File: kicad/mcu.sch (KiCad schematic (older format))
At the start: 35 parts, among them J4 UEXT, J7 6P6C, J8 ST_Nucleo_SWD_5p, U1 STM32L072CZTx, U4 D1213A-04SO

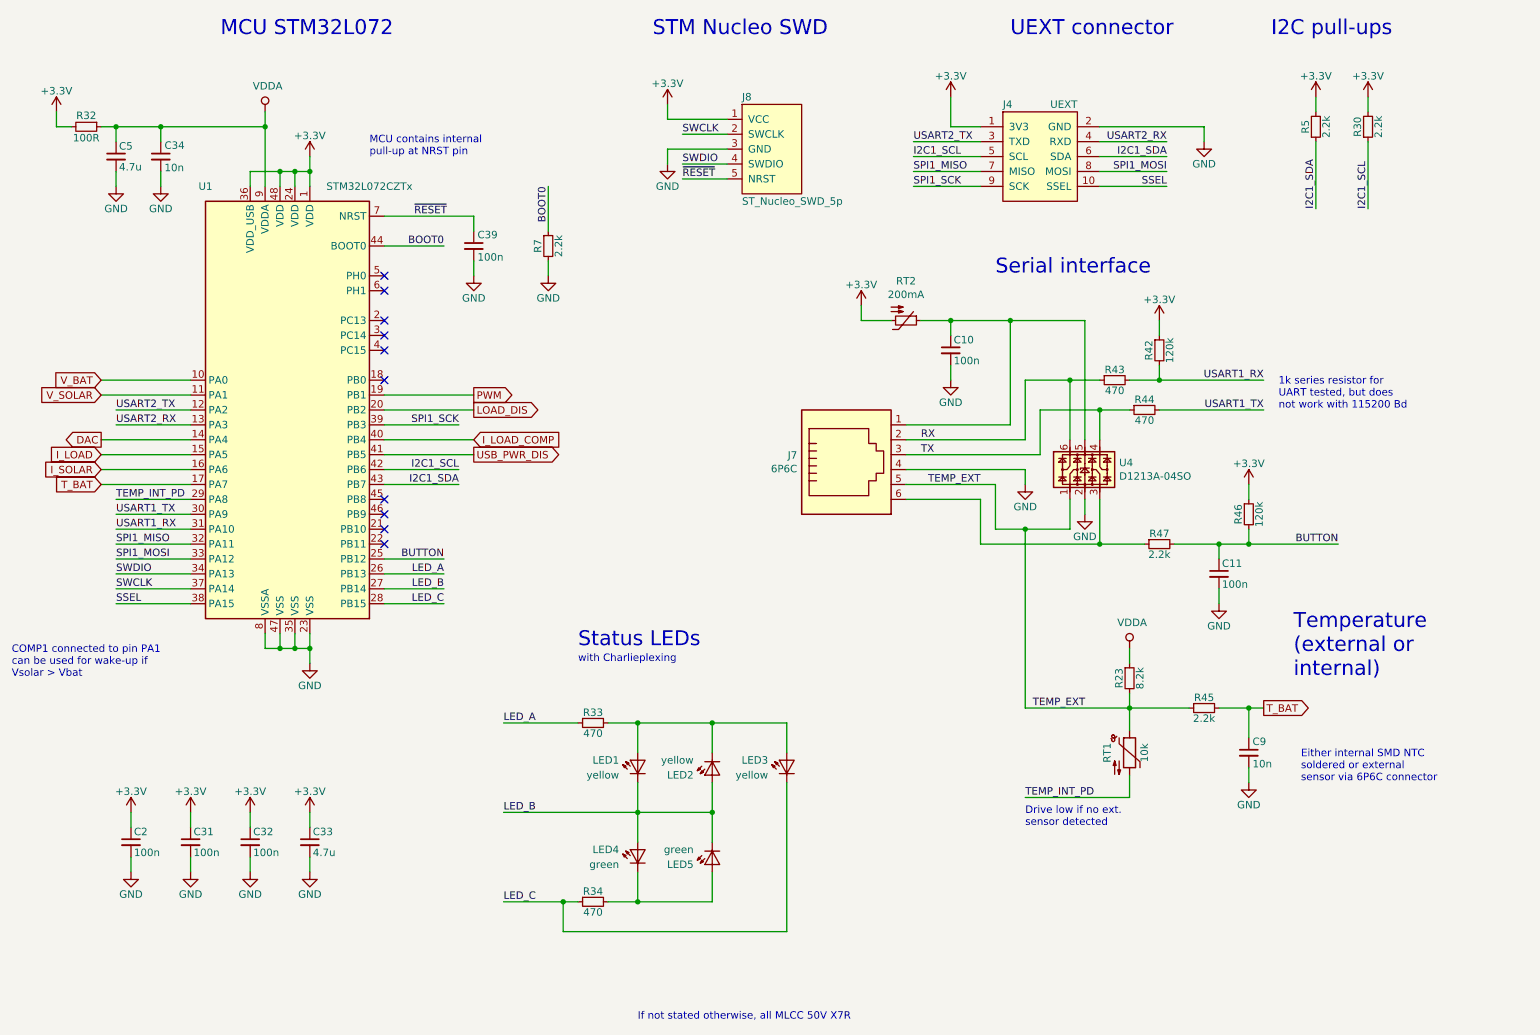
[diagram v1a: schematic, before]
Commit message: Improved power supply and exposed BOOT0 pin
- BOOT0 pin connected to BUTTON wire to allow firmware upgrade via LS.one port
- Additional emitter follower for 3V3 power supply to increase margin to 30V absolute max. rating of LDO in case of 24V battery
- Corners adjusted to match shape of MPPT 1210 HUS
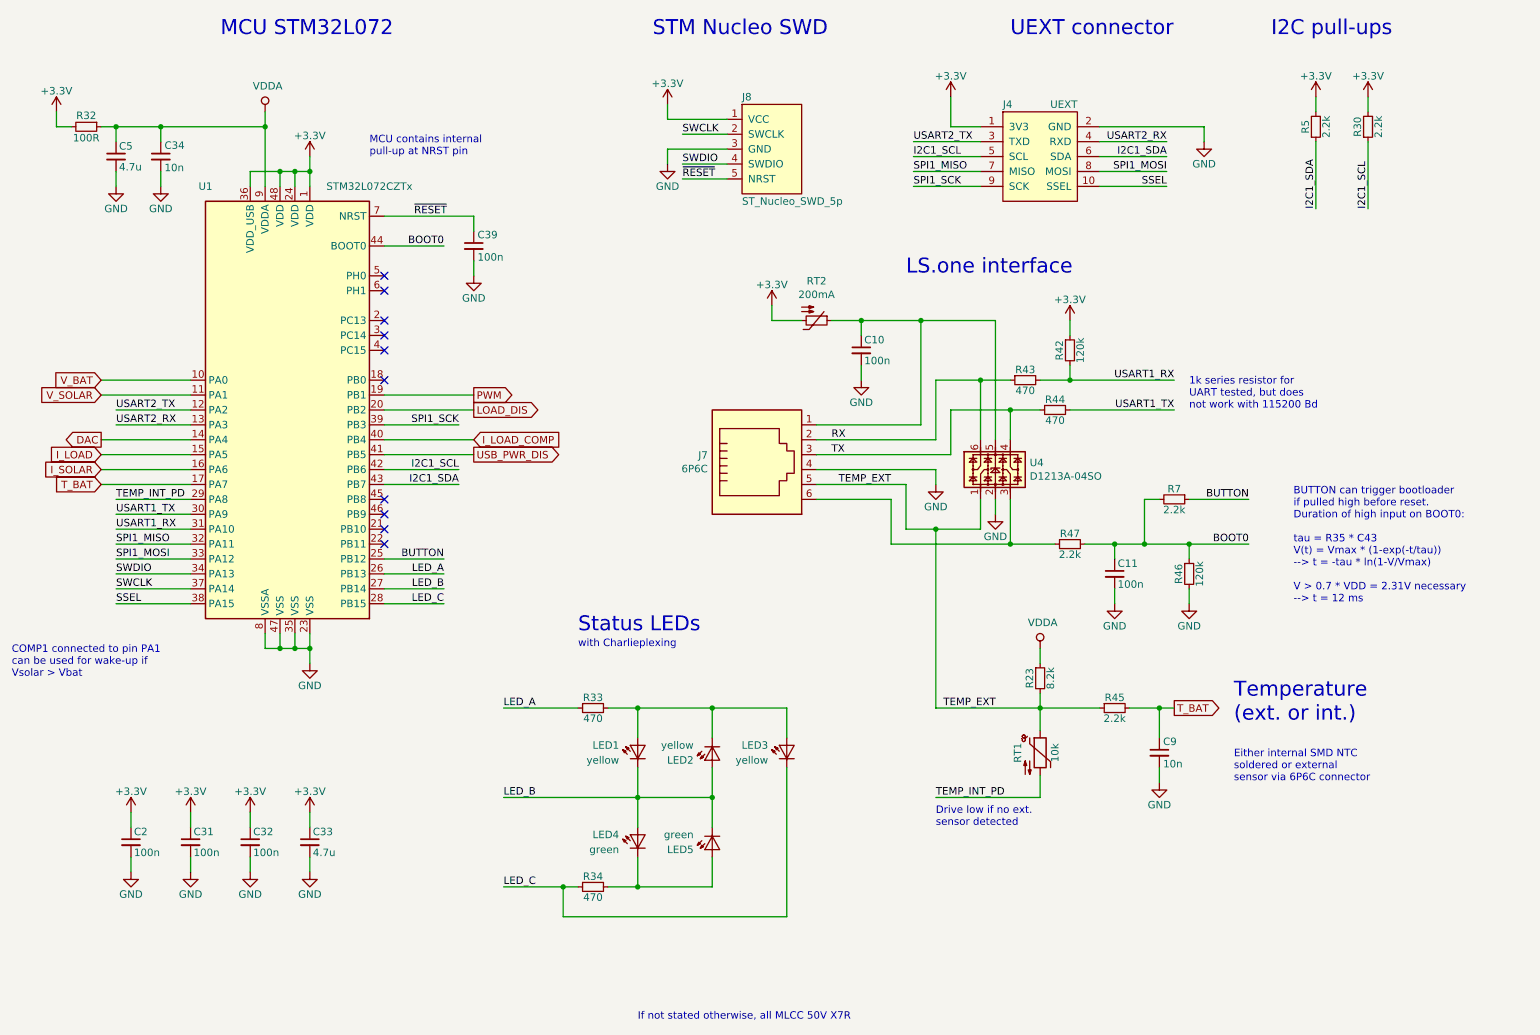
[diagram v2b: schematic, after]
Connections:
- net +3V3: no longer R46.1
- net BOOT0: now also C11.1, R46.1, R47.2, R7.2; no longer R7.1
- net BUTTON: now also R7.1; no longer C11.1, R46.2, R47.2
- net GND: now also R46.2; no longer R7.2
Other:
- note added: "BUTTON can trigger bootloader\nif pulled high before reset.\nDuration of high input on BOOT0:\n\ntau = R35 * C43\nV(t) = Vmax * (1-exp(-t/tau))\n--> t = -tau * ln(1-V/Vmax)\n\nV > 0.7 * VDD = 2.31V necessary\n--> t = 12 ms"
- note added: "LS.one interface"
- note added: "Temperature\n(ext. or int.)"
- note removed: "Serial interface"
- note removed: "Temperature\n(external or \ninternal)"
- moved on the sheet: C10, C11, C9, J7, LED1, LED2, LED3, LED4, LED5, R23, R33, R34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
